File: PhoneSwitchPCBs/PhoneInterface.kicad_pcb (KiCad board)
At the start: 2 copper layers, 101.6 x 50.8 mm, 53 parts, among them J1 Interface, J2 6P2C, K1 EC2-5NU, K2 EC2-5NU, K3 EC2-5NU, K4 EC2-5NU, K5 EC2-5NU, Q1 PHPT61003PYX, Q2 PHPT61003NYX, Q3 XP231N02013R-G, Q4 XP231N02013R-G, Q5 XP231N02013R-G, Q6 XP231N02013R-G, U1 TCMD1000, U2 NL17SZ14DBVT1G

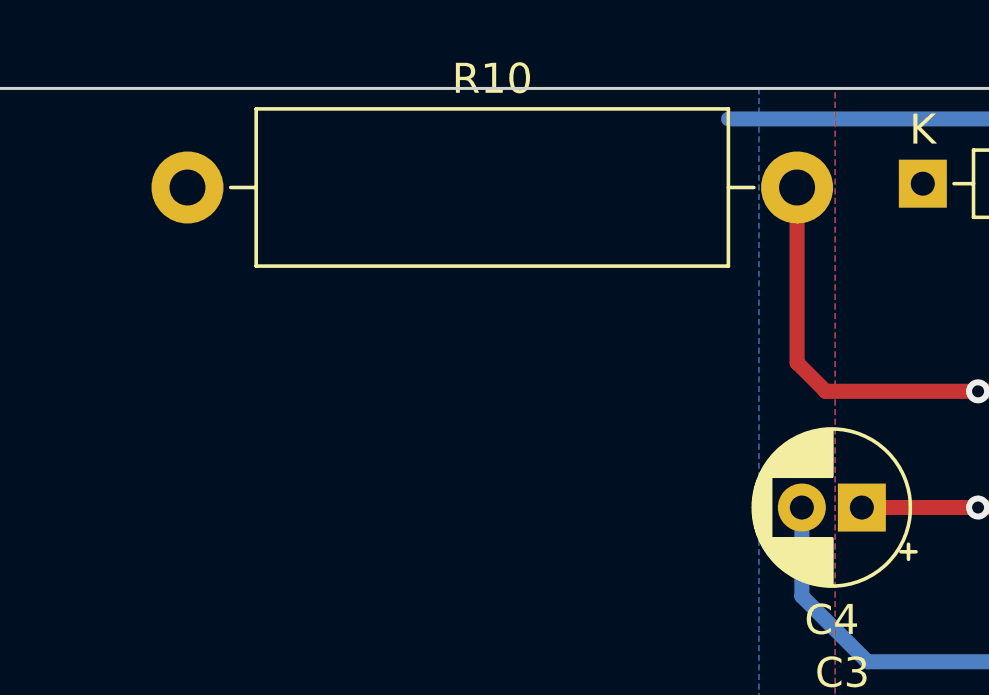
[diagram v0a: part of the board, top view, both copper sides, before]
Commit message: Start NEW more carefully laid out PCB.  Completed gyrator sections.
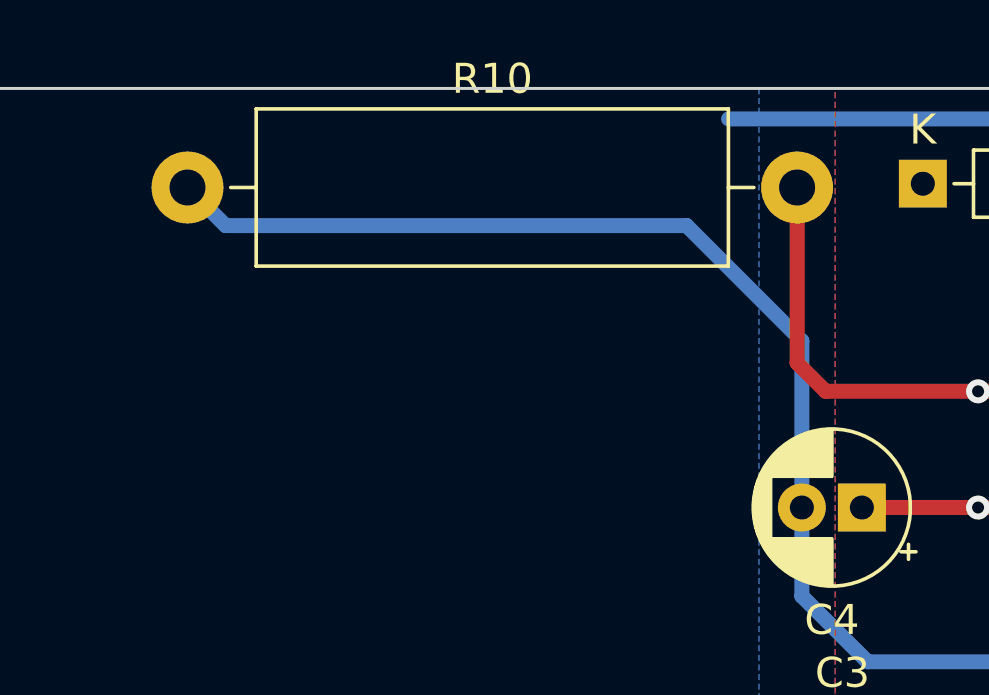
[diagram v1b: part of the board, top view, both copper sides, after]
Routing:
- net Net-(C4-Pad2): track 12.1 -> 40.3 mm
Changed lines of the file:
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@@
     (thickness 1.6)
     (drawings 14)
-    (tracks 67)
+    (tracks 71)
     (zones 0)
     (modules 53)
@@
   (segment (start 173.768 92.488) (end 173.768 89.535) (width 0.499872) (layer B.Cu) (net 7))
   (segment (start 175.956 94.676) (end 173.768 92.488) (width 0.499872) (layer B.Cu) (net 7))
+  (segment (start 173.768 89.535) (end 173.768 83.979) (width 0.499872) (layer B.Cu) (net 7))
+  (segment (start 173.768 83.979) (end 169.926 80.137) (width 0.499872) (layer B.Cu) (net 7))
+  (segment (start 154.559 80.137) (end 153.289 78.867) (width 0.499872) (layer B.Cu) (net 7))
+  (segment (start 169.926 80.137) (end 154.559 80.137) (width 0.499872) (layer B.Cu) (net 7))
   (segment (start 187.123 85.598) (end 185.547 87.174) (width 0.499872) (layer B.Cu) (net 8))
   (segment (start 185.547 87.985) (end 183.997 89.535) (width 0.499872) (layer B.Cu) (net 8))

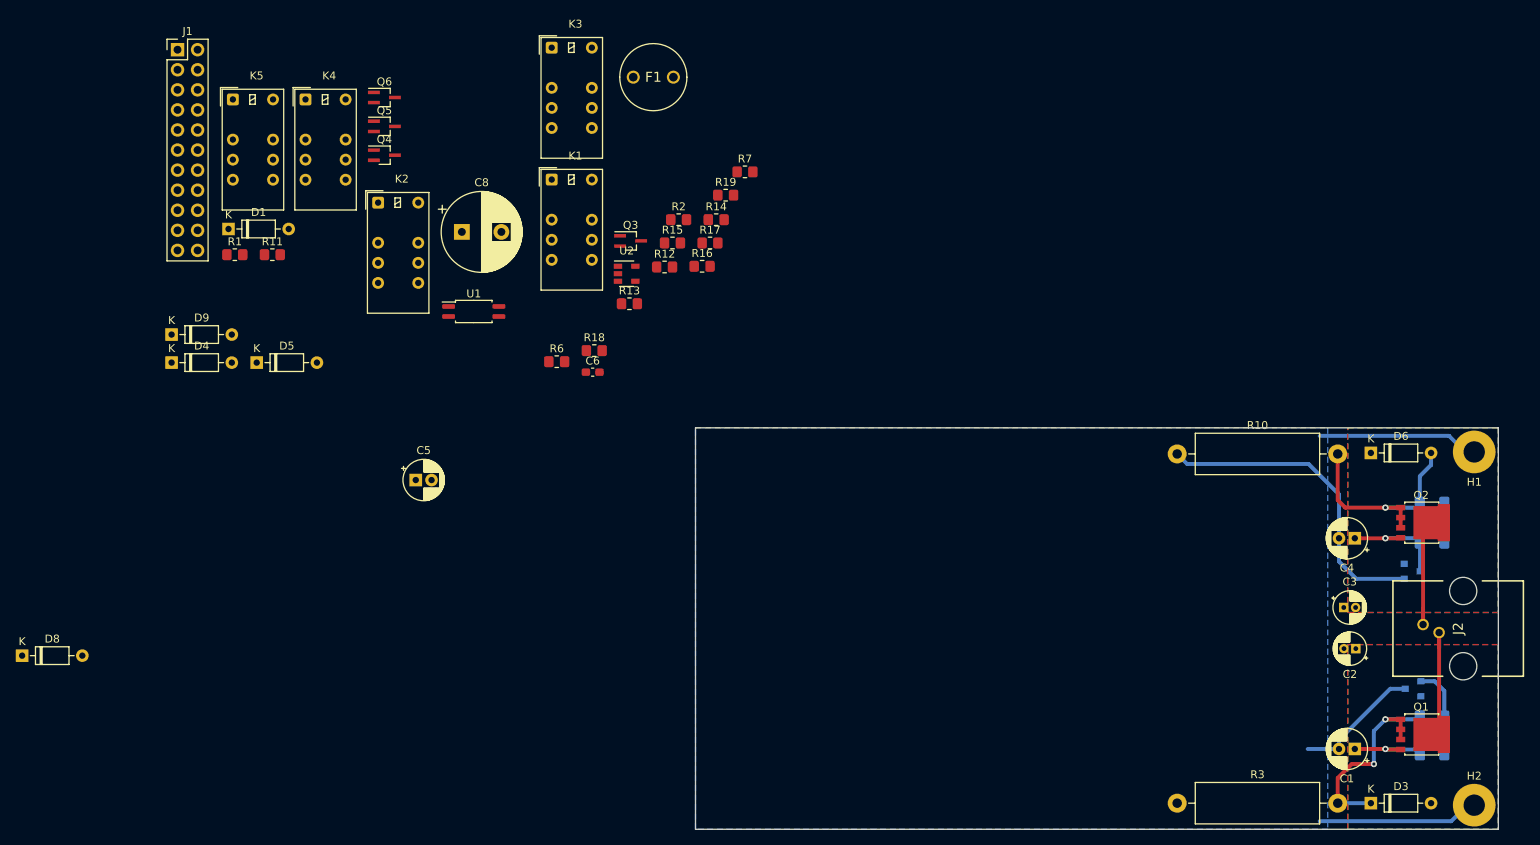
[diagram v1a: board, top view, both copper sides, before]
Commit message: More progress, added two extra mounting holes
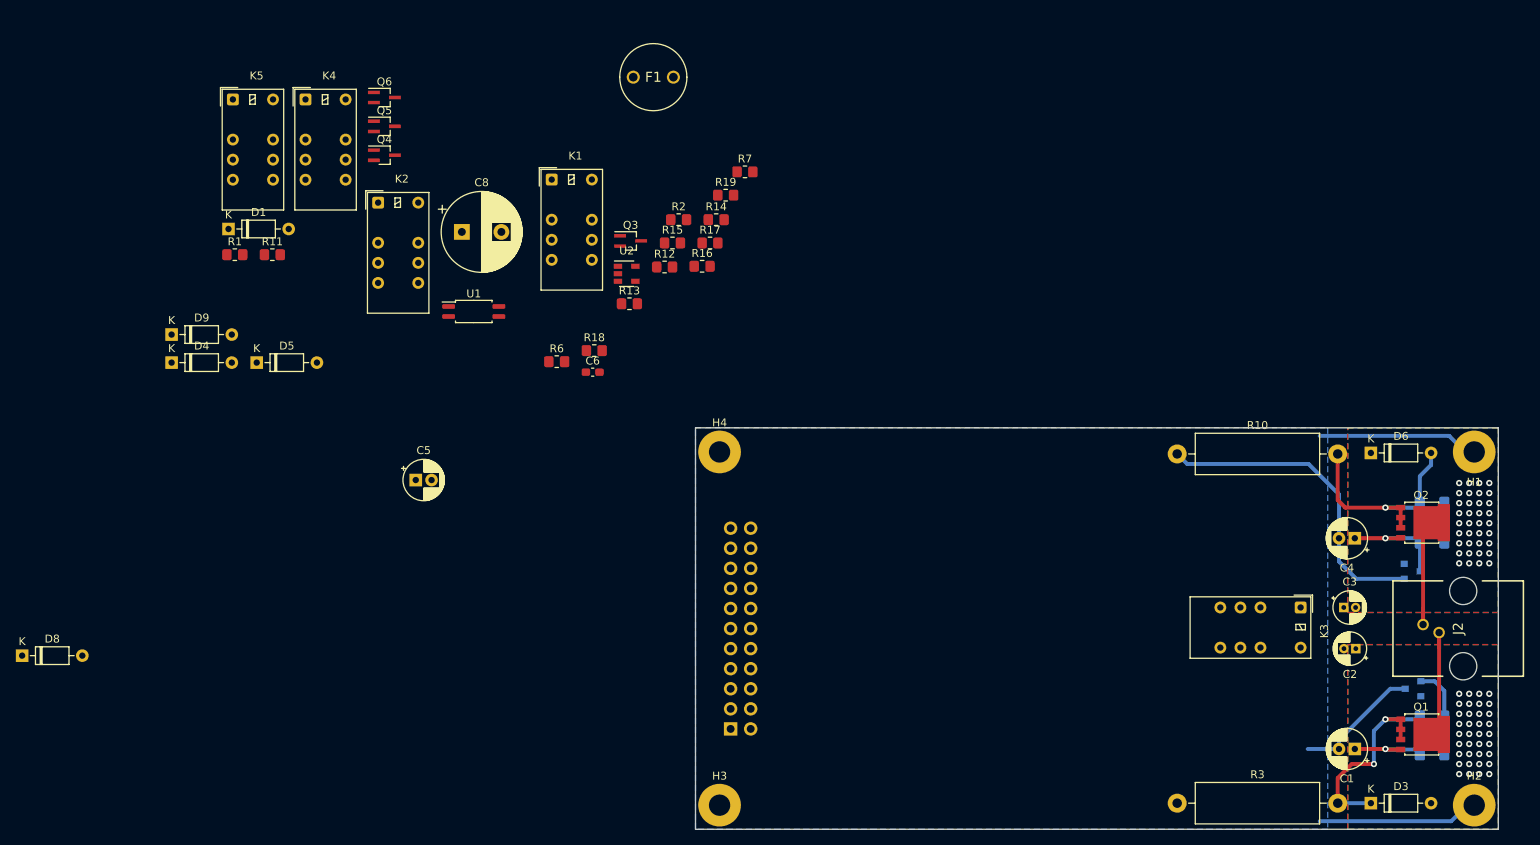
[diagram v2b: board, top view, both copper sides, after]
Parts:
- added H3: MNT1, MountingHole:MountingHole_2.7mm_M2.5_Pad, F.Cu at (95.4, 123.3)
- added H4: MNT1, MountingHole:MountingHole_2.7mm_M2.5_Pad, F.Cu at (95.4, 78.6)
- J1: moved to B.Cu
- moved K3 118.3 mm to (168.9, 98.3), turned to 270 degrees
- moved J1 110.9 mm to (96.8, 113.7)
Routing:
- net /TIP: vias 0 -> 36
- net /RING: vias 0 -> 36

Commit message: Finished routing tracks
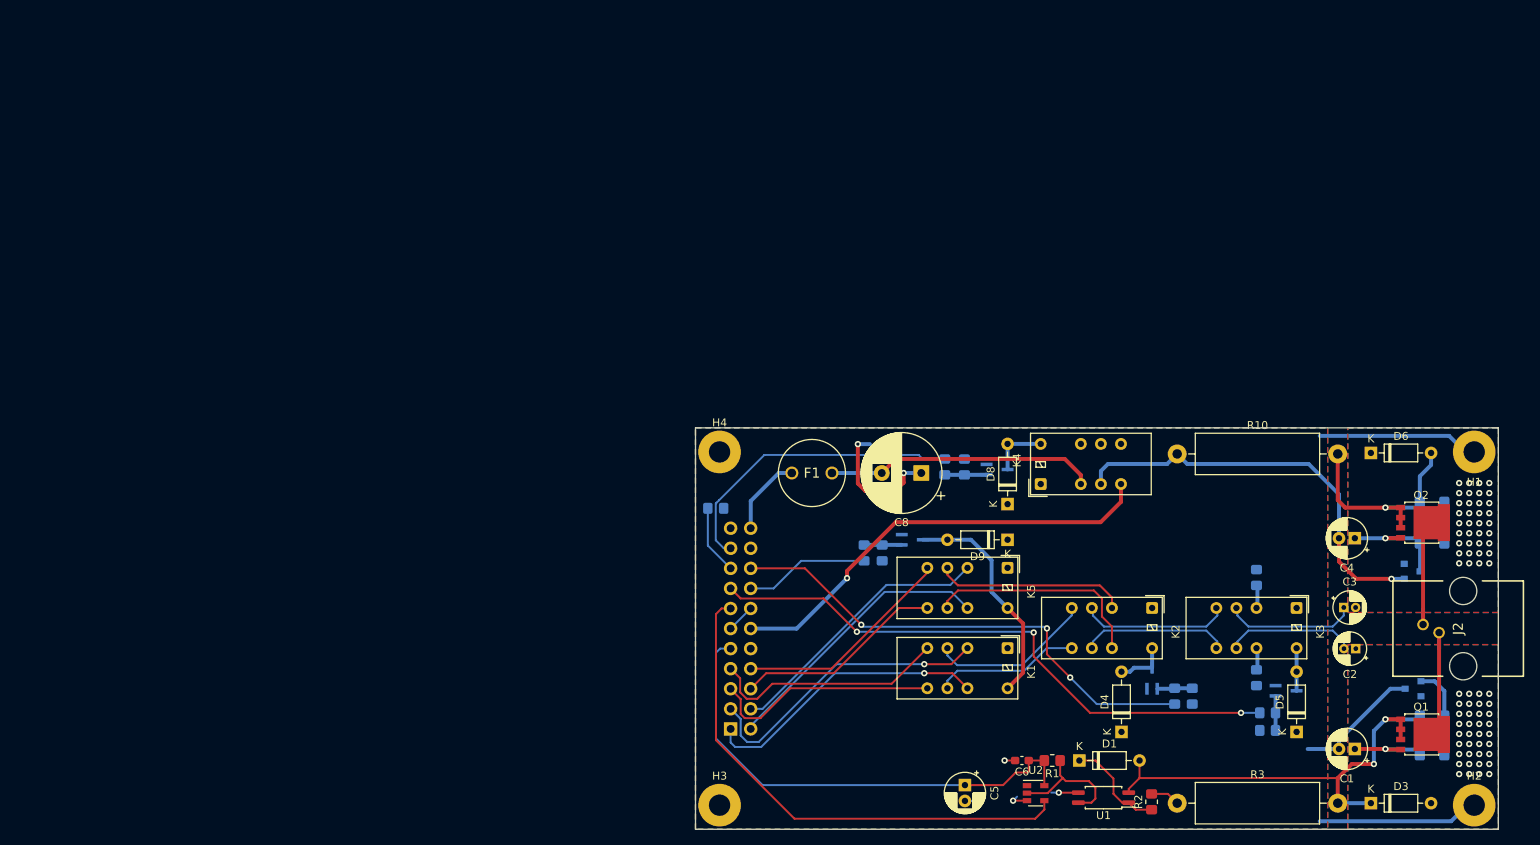
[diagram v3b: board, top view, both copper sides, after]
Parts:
- Q3, Q4, Q5, Q6, R11, R12, R13, R14, R15, R16, R17, R18, R19, R6, R7: moved to B.Cu
- moved D5 139.7 mm to (168.4, 114.0), turned to 90 degrees
- moved R11 138.7 mm to (164.7, 111.6)
- moved D4 129.0 mm to (146.2, 114.0), turned to 90 degrees
- moved D1 127.0 mm to (140.9, 117.7)
- moved D8 126.2 mm to (131.8, 85.2), turned to 90 degrees
- moved Q6 121.8 mm to (150.1, 107.3), turned to 90 degrees
- moved R1 121.7 mm to (137.5, 117.7), turned to 180 degrees
- moved K5 114.6 mm to (131.8, 93.3), turned to 270 degrees
- moved K2 110.6 mm to (150.1, 98.4), turned to 270 degrees
- moved D9 108.9 mm to (131.8, 89.7), turned to 180 degrees
- moved K4 105.0 mm to (136.0, 82.7), turned to 90 degrees
- moved U1 100.7 mm to (144.0, 122.4), turned to 180 degrees
- moved Q3 100.6 mm to (167.1, 108.8)
- moved R6 97.2 mm to (163.3, 107.2), turned to 90 degrees
- moved R13 97.2 mm to (164.7, 113.9)
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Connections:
- J1 pad 13: /AUDE -> /RTRIP
- J1 pad 15: /RTRIP -> /AUDE
- K1 pad 10: Net-(J1-Pad3) -> Net-(J1-Pad1)
- K1 pad 3: Net-(J1-Pad1) -> Net-(J1-Pad3)
- K1 pad 5: Net-(J1-Pad5) -> Net-(J1-Pad7)
- K1 pad 8: Net-(J1-Pad7) -> Net-(J1-Pad5)
- K5 pad 10: Net-(J1-Pad4) -> Net-(J1-Pad2)
- K5 pad 3: Net-(J1-Pad2) -> Net-(J1-Pad4)
- K5 pad 5: Net-(J1-Pad6) -> Net-(J1-Pad8)
- K5 pad 8: Net-(J1-Pad8) -> Net-(J1-Pad6)
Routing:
- net /AUDE: track 0.00 -> 75.3 mm, vias 0 -> 3
- net /RTRIP: track 0.00 -> 65.4 mm
- net /LINE: track 0.00 -> 62.7 mm, vias 0 -> 3
- net +3V3: track 0.00 -> 62.2 mm
- net /VRING: track 0.00 -> 56.3 mm, vias 0 -> 1
- net /RINGE: track 0.00 -> 38.7 mm
- net Net-(J1-Pad3): track 0.00 -> 37.9 mm, vias 0 -> 1
- net Net-(J1-Pad1): track 0.00 -> 36.6 mm, vias 0 -> 1
- net Net-(J1-Pad2): track 0.00 -> 35.7 mm
- net Net-(J1-Pad4): track 0.00 -> 34.8 mm
- net -48V: track 0.00 -> 34.2 mm
- net GND: track 57.0 -> 89.6 mm, vias 0 -> 5
- net Net-(J1-Pad7): track 0.00 -> 30.2 mm
- net Net-(D1-Pad2): track 27.8 -> 57.6 mm
- net Net-(J1-Pad5): track 0.00 -> 29.1 mm
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- added copper zone on F.Cu, net +5V

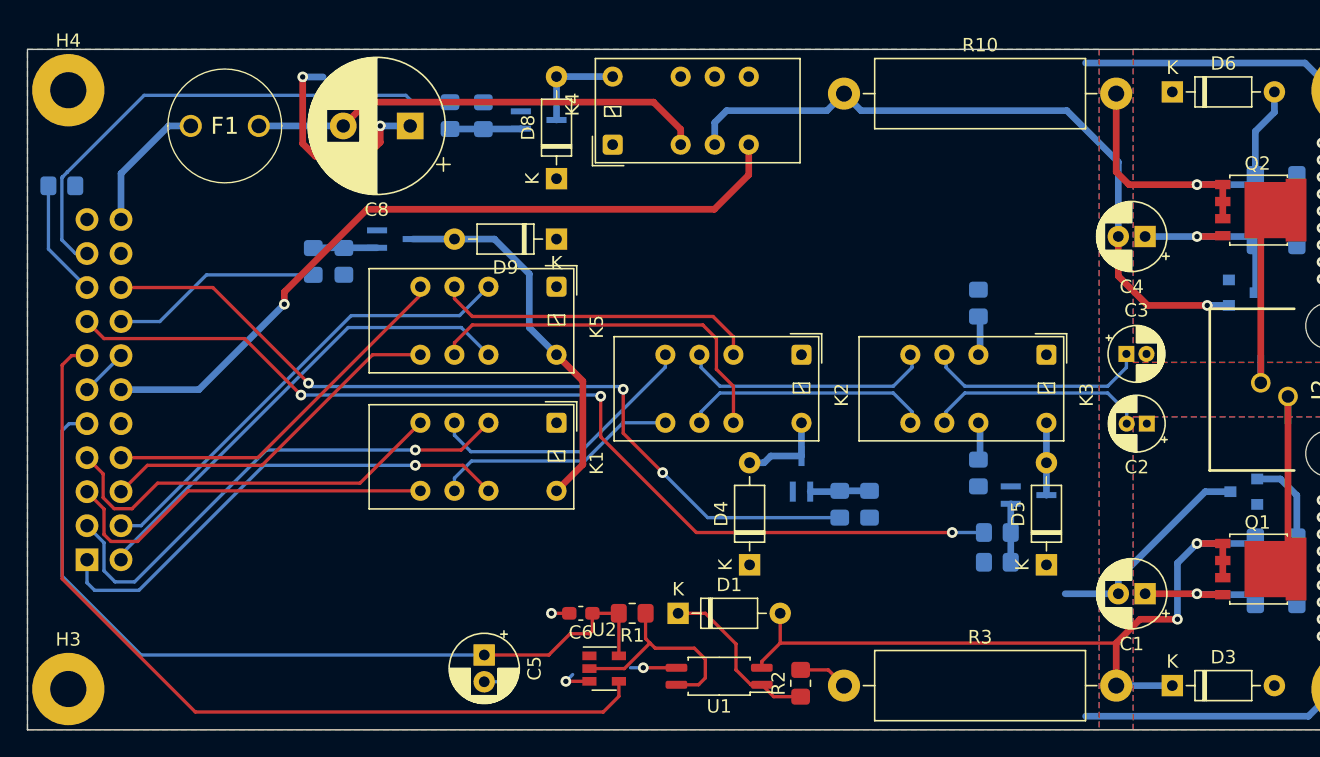
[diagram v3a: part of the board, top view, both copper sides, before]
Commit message: Finalize PCB, move around silkscreen markings
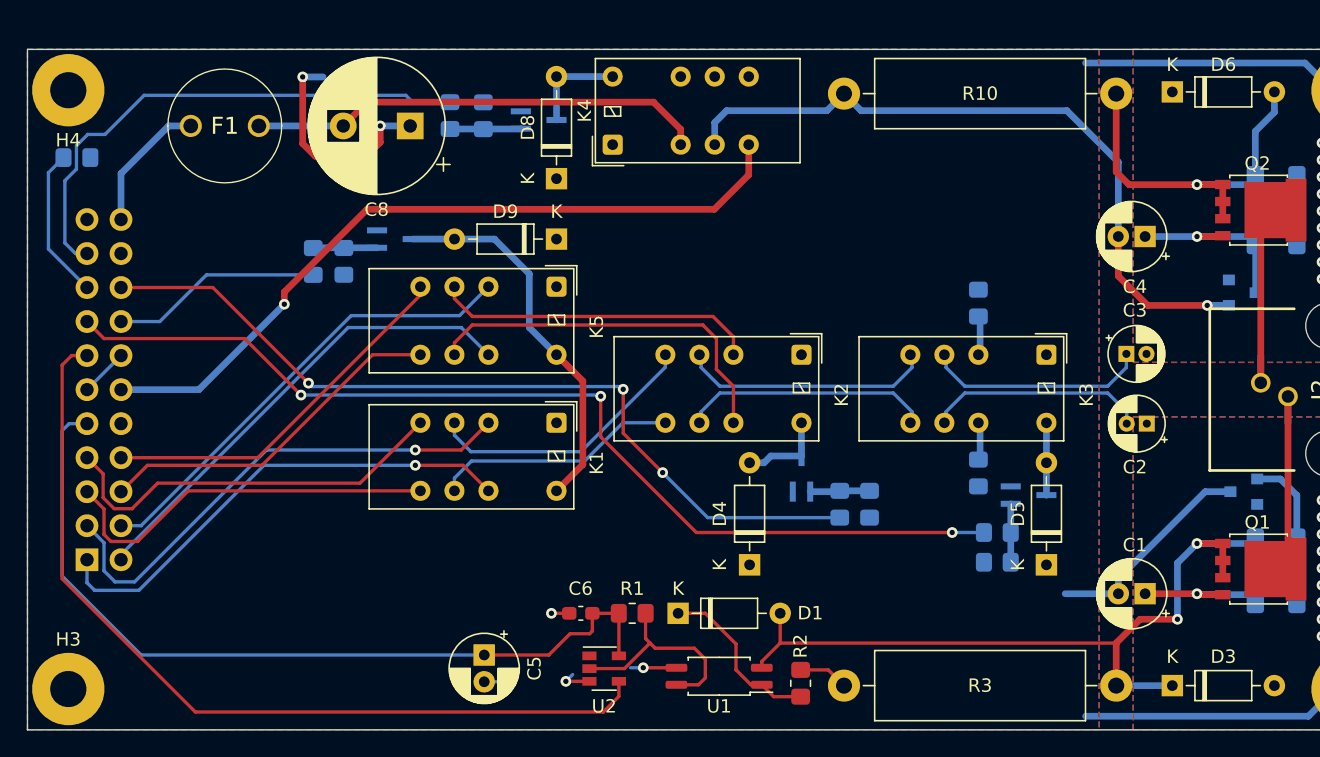
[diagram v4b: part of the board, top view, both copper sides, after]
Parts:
- moved R19 2.39 mm to (96.0, 83.6)
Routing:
- net /CINST: track 8.79 -> 11.4 mm
- net /RINGE: track 38.7 -> 39.3 mm
